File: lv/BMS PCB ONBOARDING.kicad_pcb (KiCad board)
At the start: 4 copper layers, 0 parts

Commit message: UPDATE 6: U1 core placement — VC/CB ladder, balancing staircase, and per-pin rail decoupling
Chip wiring:
- U1 anchored at the centre of the core field, with every bypass cap now
  sitting at the pin it belongs to. LDOIN, NEG5V, AVSS, BAT and CVDD each
  have their cap on the pin, so the loop closes at the pin instead of
  somewhere down a trace.
- The internal-LDO/reference caps (DVDD, TSREF, AVDD, REFHP) came in from
  the far corner of the board toward U1, but they are still not at their
  pins. That is the worst placement problem left on the board.
- Rail rework from UPDATE 5 is now true on the board, checked by net:
    CVDD  = the bulk cap plus the housekeeping pull-ups, the test point
            and the comms connector
    TSREF = the bypass cap and its test point only
- CVDD still has no high-frequency bypass beside its bulk cap, and NFAULT
  still has no pull-up - the test point is the only other pad on that net.

Footprints fixed:
- Nothing to fix: no footprint link on the board changed.
- Carried over from UPDATE 5 and re-verified on the board: the VC/CB sense
  resistor is back on the same hand-solder footprint as the rest of the
  ladder, the common-mode chokes resolve, the Nano-Fit connectors resolve
  to the Nano-Fit footprint, the pre-regulator transistor resolves, and
  every netlist part still resolves.

Blocks on the sheet:
- Whole board re-placed: every footprint moved, none added, none removed,
  netlist unchanged - pure placement, the schematic was not touched.
- Core field around U1 now holds the VC/CB sense resistors, the balancing
  resistors and the ladder caps: the filter and balancing staircase that
  UPDATE 5 could only list as pending.
- Pull-up row consolidated above U1 - the GPIO, ALERT and bus pull-ups
  pulled out of the scatter they were left in, now close to their pins and
  all on CVDD.
- Comms termination left at the connector end, far from U1 - correct, that
  network belongs at the comms conne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
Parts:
- added C1: .47uF, Capacitor_SMD:C_0603_1608Metric, F.Cu at (55.8, 74.8)
- added C10: .47uF, Capacitor_SMD:C_0603_1608Metric, F.Cu at (64.8, 91.2)
- added C11: .47uF, Capacitor_SMD:C_0603_1608Metric, F.Cu at (63.2, 89.5)
- added C12: .47uF, Capacitor_SMD:C_0603_1608Metric, F.Cu at (60.0, 87.5)
- added C19: .47uF, Capacitor_SMD:C_0603_1608Metric, F.Cu at (71.2, 91.2)
- added C2: .47uF, Capacitor_SMD:C_0603_1608Metric, F.Cu at (54.0, 76.3)
- added C20: .47uF, Capacitor_SMD:C_0603_1608Metric, F.Cu at (73.0, 89.5)
- added C201: 10nF, GCM188R72A103KA37J:CAPC1608X90N, F.Cu at (62.3, 70.2)
- added C202: 0.1uF, GCM155R71A104KA55D:CAP_GCM15_1p05X0p55X0p55_MUR-L, F.Cu at (75.2, 76.5)
- added C203: 1uF, C0603C105K8RACAUTO:CAPC18095_95N_KEM-L, F.Cu at (51.9, 57.5)
- added C205: 1uF, C0603C105K8RACAUTO:CAPC18095_95N_KEM-L, F.Cu at (52.9, 59.5)
- added C207: 2.2uF, C0603C105K8RACAUTO:CAPC18095_95N_KEM-L, F.Cu at (51.9, 62.0)
- added C208: 0.1uF, GCM155R71A104KA55D:CAP_GCM15_1p05X0p55X0p55_MUR-L, F.Cu at (74.8, 74.8)
- added C209: 4.7uF, C2012X7R1A475M125AC:CAP_2012_TDK-L, F.Cu at (77.2, 77.1)
- added C21: .47uF, Capacitor_SMD:C_0603_1608Metric, F.Cu at (75.0, 80.0)
- added C210: 1uF, C0603C105K8RACAUTO:CAPC18095_95N_KEM-L, F.Cu at (51.9, 64.2)
- added C22: .47uF, Capacitor_SMD:C_0603_1608Metric, F.Cu at (76.8, 82.5)
- added C23: .47uF, Capacitor_SMD:C_0603_1608Metric, F.Cu at (78.8, 81.0)
- added C24: .47uF, Capacitor_SMD:C_0603_1608Metric, F.Cu at (59.2, 73.5)
- added C25: .47uF, Capacitor_SMD:C_0603_1608Metric, F.Cu at (57.5, 74.9)
- added C26: .47uF, Capacitor_SMD:C_0603_1608Metric, F.Cu at (57.5, 78.2)
- added C27: .47uF, Capacitor_SMD:C_0603_1608Metric, F.Cu at (59.2, 76.8)
- added C28: .47uF, Capacitor_SMD:C_0603_1608Metric, F.Cu at (57.5, 84.7)
- added C29: .47uF, Capacitor_SMD:C_0603_1608Metric, F.Cu at (59.2, 83.3)
- added C3: .47uF, Capacitor_SMD:C_0603_1608Metric, F.Cu at (55.8, 81.2)
- added C30: .47uF, Capacitor_SMD:C_0603_1608Metric, F.Cu at (57.5, 81.5)
- added C31: .47uF, Capacitor_SMD:C_0603_1608Metric, F.Cu at (59.2, 80.0)
- added C32: .47uF, Capacitor_SMD:C_0603_1608Metric, F.Cu at (75.0, 83.5)
- added C33: .47uF, Capacitor_SMD:C_0603_1608Metric, F.Cu at (72.5, 86.0)
- added C34: .47uF, Capacitor_SMD:C_0603_1608Metric, F.Cu at (70.5, 87.8)
- added C35: .47uF, Capacitor_SMD:C_0603_1608Metric, F.Cu at (69.3, 86.0)
- added C36: .47uF, Capacitor_SMD:C_0603_1608Metric, F.Cu at (67.2, 87.8)
- added C37: .47uF, Capacitor_SMD:C_0603_1608Metric, F.Cu at (66.0, 86.0)
- added C38: .47uF, Capacitor_SMD:C_0603_1608Metric, F.Cu at (64.0, 87.8)
- added C39: .47uF, Capacitor_SMD:C_0603_1608Metric, F.Cu at (62.7, 86.0)
- added C4: .47uF, Capacitor_SMD:C_0603_1608Metric, F.Cu at (54.0, 79.5)
- added C40: .47uF, Capacitor_SMD:C_0603_1608Metric, F.Cu at (81.8, 82.8)
- added C41: 470nF, Capacitor_SMD:C_0603_1608Metric, F.Cu at (58.5, 71.0)
- added C5: .47uF, Capacitor_SMD:C_0603_1608Metric, F.Cu at (68.0, 91.2)
- added C6: .47uF, Capacitor_SMD:C_0603_1608Metric, F.Cu at (55.8, 78.0)
- added C602: 0.22uF, GCM31MR72A224KA37L:G-31_MUR-L, F.Cu at (224.3, 70.5)
- added C7: .47uF, Capacitor_SMD:C_0603_1608Metric, F.Cu at (54.0, 82.8)
- added C701: 2200pF, 1206J2K00222KXR:CAPC3216X160N, F.Cu at (229.7, 105.0)
- added C702: 2200pF, 1206J2K00222KXR:CAPC3216X160N, F.Cu at (229.7, 108.4)
- added C703: 220pF, CL10B221JB8NNNC:CAP_CL10_SAM-L, F.Cu at (230.8, 75.0)
- added C704: 220pF, CL10B221JB8NNNC:CAP_CL10_SAM-L, F.Cu at (230.8, 77.2)
- added C705: 220pF, CL10B221JB8NNNC:CAP_CL10_SAM-L, F.Cu at (230.8, 79.4)
- added C706: 220pF, CL10B221JB8NNNC:CAP_CL10_SAM-L, F.Cu at (230.8, 81.6)
- added C707: 2200pF, 1206J2K00222KXR:CAPC3216X160N, F.Cu at (229.7, 111.7)
- added C708: 2200pF, 1206J2K00222KXR:CAPC3216X160N, F.Cu at (229.7, 115.1)
- added C8: .47uF, Capacitor_SMD:C_0603_1608Metric, F.Cu at (69.8, 89.5)
- added C9: .47uF, Capacitor_SMD:C_0603_1608Metric, F.Cu at (66.5, 89.5)
- added D701: 24V, Package_TO_SOT_SMD:SOT-23, F.Cu at (191.9, 107.3)
- added D702: 24V, Package_TO_SOT_SMD:SOT-23, F.Cu at (191.9, 111.7)
- added FL701: 470uH, 744242471:744242471, F.Cu at (226.1, 91.8)
- added FL702: 470uH, 744242471:744242471, F.Cu at (226.1, 98.2)
- added J3: 512810598, FS_4_Global_Footprint_Library:512810598, F.Cu at (224.5, 77.8)
- added J4: 1053131202, FS_4_Global_Footprint_Library:Nanofit-1054301202-1x2SMD90Deg, F.Cu at (203.6, 96.7)
- added J5: 512810598, FS_4_Global_Footprint_Library:512810598, F.Cu at (224.5, 85.1)
- added J6: 1053131202, FS_4_Global_Footprint_Library:Nanofit-1054301202-1x2SMD90Deg, F.Cu at (215.0, 96.7)
- added J701: 430450200, 0430450200:CON_430450200_MOL, F.Cu at (203.8, 63.2)
- added J702: 430450200, 0430450200:CON_430450200_MOL, F.Cu at (215.1, 63.2)
- added Q1: ZXTN25100DGTA, footprintsZXTN25100DGTA:SOT223_DIO, F.Cu at (181.9, 109.8)
- added R1: 10k, Resistor_SMD:R_0805_2012Metric, F.Cu at (72.2, 63.4)
- added R100: 100, Resistor_SMD:R_0805_2012Metric_Pad1.20x1.40mm_HandSolder, F.Cu at (56.2, 97.8)
- added R101: 10, Resistor_SMD:R_2512_6332Metric, F.Cu at (48.5, 90.8)
- added R102: 100, Resistor_SMD:R_0805_2012Metric_Pad1.20x1.40mm_HandSolder, F.Cu at (41.8, 95.0)
- added R103: 100, Resistor_SMD:R_0805_2012Metric_Pad1.20x1.40mm_HandSolder, F.Cu at (41.5, 90.8)
- added R116: 10, Resistor_SMD:R_2512_6332Metric, F.Cu at (73.8, 96.5)
- added R117: 100, Resistor_SMD:R_0805_2012Metric_Pad1.20x1.40mm_HandSolder, F.Cu at (73.8, 103.0)
- added R118: 10, Resistor_SMD:R_2512_6332Metric, F.Cu at (78.0, 96.5)
- added R119: 100, Resistor_SMD:R_0805_2012Metric_Pad1.20x1.40mm_HandSolder, F.Cu at (78.0, 103.0)
- added R12: 5k, Resistor_SMD:R_0805_2012Metric_Pad1.20x1.40mm_HandSolder, F.Cu at (67.8, 63.5)
- added R120: 10, Resistor_SMD:R_2512_6332Metric, F.Cu at (78.8, 87.2)
- added R121: 10, Resistor_SMD:R_2512_6332Metric, F.Cu at (82.2, 96.5)
- added R122: 100, Resistor_SMD:R_0805_2012Metric_Pad1.20x1.40mm_HandSolder, F.Cu at (84.8, 87.2)
- added R123: 100, Resistor_SMD:R_0805_2012Metric_Pad1.20x1.40mm_HandSolder, F.Cu at (82.2, 103.0)
- added R124: 100, Resistor_SMD:R_0805_2012Metric_Pad1.20x1.40mm_HandSolder, F.Cu at (82.2, 77.8)
- added R125: 10, Resistor_SMD:R_2512_6332Metric, F.Cu at (85.5, 79.8)
- added R14: 5k, Resistor_SMD:R_0805_2012Metric_Pad1.20x1.40mm_HandSolder, F.Cu at (63.2, 63.5)
- added R2: 10k, Resistor_SMD:R_0805_2012Metric, F.Cu at (69.6, 58.8)
- added R201: 30, ERJ-3EKF30R0V:RC0603N_PAN-L, F.Cu at (61.5, 72.6)
- added R3: 10k, Resistor_SMD:R_0805_2012Metric, F.Cu at (70.0, 63.5)
- added R4: 10k, Resistor_SMD:R_0805_2012Metric, F.Cu at (63.0, 48.1)
- added R5: 5k, Resistor_SMD:R_0805_2012Metric, F.Cu at (63.0, 51.1)
- added R603: 100, CRCW2010100RFKEF:RES_CRCW_2010-L, F.Cu at (180.1, 116.5)
- added R604: 200, Resistor_SMD:R_2010_5025Metric, F.Cu at (193.2, 116.0)
- added R7: 5k, Resistor_SMD:R_0805_2012Metric, F.Cu at (63.0, 54.0)
- added R701: 0, CRCW08050000Z0EAHP:RES_CRCW_0805_VIS-L, F.Cu at (222.9, 59.4)
- added R702: 0, CRCW08050000Z0EAHP:RES_CRCW_0805_VIS-L, F.Cu at (222.9, 62.1)
- added R703: 0, RC0603JR-070RL:RC0603N_YAG-L, F.Cu at (196.0, 106.1)
- added R704: 0, RC0603JR-070RL:RC0603N_YAG-L, F.Cu at (196.0, 108.2)
- added R705: 0, CRCW08050000Z0EAHP:RES_CRCW_0805_VIS-L, F.Cu at (222.9, 64.9)
- added R706: 0, CRCW08050000Z0EAHP:RES_CRCW_0805_VIS-L, F.Cu at (222.9, 67.6)
- added R707: 51, CRCW060351R0JNEA:RC0603N_VIS-L, F.Cu at (219.0, 77.1)
- added R708: 51, CRCW060351R0JNEA:RC0603N_VIS-L, F.Cu at (219.0, 79.2)
- added R709: 0, CRCW08050000Z0EAHP:RES_CRCW_0805_VIS-L, F.Cu at (226.6, 59.4)
- added R710: 0, CRCW08050000Z0EAHP:RES_CRCW_0805_VIS-L, F.Cu at (226.6, 62.1)
- added R711: 1k, ERJ-3EKF1001V:RC0603N_PAN-L, F.Cu at (219.0, 81.3)
- added R712: 1k, ERJ-3EKF1001V:RC0603N_PAN-L, F.Cu at (219.0, 83.4)
- added R713: 0, CRCW08050000Z0EAHP:RES_CRCW_0805_VIS-L, F.Cu at (226.6, 64.9)
- added R714: 0, CRCW08050000Z0EAHP:RES_CRCW_0805_VIS-L, F.Cu at (226.6, 67.6)
- added R715: 0, CRCW08050000Z0EAHP:RES_CRCW_0805_VIS-L, F.Cu at (230.3, 59.4)
- added R716: 0, CRCW08050000Z0EAHP:RES_CRCW_0805_VIS-L, F.Cu at (230.3, 62.1)
- added R717: 51, CRCW060351R0JNEA:RC0603N_VIS-L, F.Cu at (219.0, 85.5)
- added R718: 51, CRCW060351R0JNEA:RC0603N_VIS-L, F.Cu at (219.0, 87.6)
- added R719: 0, RC0603JR-070RL:RC0603N_YAG-L, F.Cu at (196.0, 110.3)
- added R720: 0, RC0603JR-070RL:RC0603N_YAG-L, F.Cu at (196.0, 112.4)
- added R721: 0, CRCW08050000Z0EAHP:RES_CRCW_0805_VIS-L, F.Cu at (230.3, 64.9)
- added R722: 0, CRCW08050000Z0EAHP:RES_CRCW_0805_VIS-L, F.Cu at (230.3, 67.6)
- added R8: 5k, Resistor_SMD:R_0805_2012Metric, F.Cu at (63.0, 57.0)
- added R80: 100, Resistor_SMD:R_0805_2012Metric_Pad1.20x1.40mm_HandSolder, F.Cu at (53.8, 72.2)
- added R81: 10, Resistor_SMD:R_2512_6332Metric, F.Cu at (59.2, 65.0)
- added R82: 10, Resistor_SMD:R_2512_6332Metric, F.Cu at (48.5, 69.5)
- added R83: 100, Resistor_SMD:R_0805_2012Metric_Pad1.20x1.40mm_HandSolder, F.Cu at (41.5, 69.5)
- added R84: 10, Resistor_SMD:R_2512_6332Metric, F.Cu at (48.5, 82.2)
- added R85: 10, Resistor_SMD:R_2512_6332Metric, F.Cu at (48.5, 78.0)
- added R86: 100, Resistor_SMD:R_0805_2012Metric_Pad1.20x1.40mm_HandSolder, F.Cu at (41.5, 82.2)
- added R87: 100, Resistor_SMD:R_0805_2012Metric_Pad1.20x1.40mm_HandSolder, F.Cu at (41.5, 78.0)
- added R88: 10, Resistor_SMD:R_2512_6332Metric, F.Cu at (65.2, 96.5)
- added R89: 10, Resistor_SMD:R_2512_6332Metric, F.Cu at (48.5, 73.8)
- added R9: 5k, Resistor_SMD:R_0805_2012Metric_Pad1.20x1.40mm_HandSolder, F.Cu at (65.5, 63.5)
- added R90: 10, Resistor_SMD:R_2512_6332Metric, F.Cu at (48.5, 86.5)
- added R91: 100, Resistor_SMD:R_0805_2012Metric_Pad1.20x1.40mm_HandSolder, F.Cu at (41.5, 73.7)
- added R92: 100, Resistor_SMD:R_0805_2012Metric_Pad1.20x1.40mm_HandSolder, F.Cu at (41.5, 86.5)
- added R93: 10, Resistor_SMD:R_2512_6332Metric, F.Cu at (69.5, 96.5)
- added R94: 100, Resistor_SMD:R_0805_2012Metric_Pad1.20x1.40mm_HandSolder, F.Cu at (69.5, 103.0)
- added R95: 10, Resistor_SMD:R_2512_6332Metric, F.Cu at (61.0, 96.5)
- added R96: 100, Resistor_SMD:R_0805_2012Metric_Pad1.20x1.40mm_HandSolder, F.Cu at (65.2, 103.0)
- added R97: 10, Resistor_SMD:R_2512_6332Metric, F.Cu at (56.2, 91.5)
- added R98: 100, Resistor_SMD:R_0805_2012Metric_Pad1.20x1.40mm_HandSolder, F.Cu at (61.0, 103.0)
- added R99: 10, Resistor_SMD:R_2512_6332Metric, F.Cu at (48.5, 95.0)
- added TP501: 5012, 5012:TP_5012, F.Cu at (215.0, 105.7)
- added TP502: 5012, 5012:TP_5012, F.Cu at (215.0, 110.4)
- added TP503: 5012, 5012:TP_5012, F.Cu at (215.0, 115.1)
- added TP504: 5012, 5012:TP_5012, F.Cu at (219.8, 105.7)
- added TP505: 5012, 5012:TP_5012, F.Cu at (219.8, 110.4)
- added TP506: 5012, 5012:TP_5012, F.Cu at (219.8, 115.1)
- added TP507: 5012, 5012:TP_5012, F.Cu at (224.5, 105.7)
- added TP508: 5012, 5012:TP_5012, F.Cu at (224.5, 110.4)
- added TP509: 5012, 5012:TP_5012, F.Cu at (224.5, 115.1)
- added U1: BQ79616PAPRQ1, footprintsBQ79616PAPRQ1:PAP0064F-IPC_A, F.Cu at (67.3, 78.0)

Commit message: UPDATE 7: board edge and mounting holes — connector half brought in as blocks
Board edge:
- The outline is on the board now, drawn as straight runs and rounded corners.
  Before this the file had no Edge.Cuts geometry at all, which is why DRC could
  not start and nothing could be plotted.
- The top-right corner is cut away: the area beyond the notch line is off the
  board, so the outline is not a plain rectangle.
- Every corner is an arc, and each mounting hole sits at the centre of one, so
  the corner relief is concentric with the fastener rather than cut beside it.
- Not closed yet: the right edge stops just short of where the next run picks
  it up, and a short segment lies on the left edge duplicating that part of it.
  Both leave free endpoints, which is what the outline check and every plot key
  off. The break is closed in the newer autosave; the duplicated segment is in
  all of them.

Mounting:
- The mounting holes are non-plated: a bare drill with no annular ring, and
  excluded from the BOM. At the tightest corners the ligament to the edge is
  thin but real; a washer up to the size the corner relief allows sits inside
  the arc, and anything wider overhangs it.
- Added on the sheet as well as the board - mounting-hole symbols with their
  own references - so schematic and board still agree after the board gained
  its footprints, and the used-designator list picked them up.

Blocks on the sheet:
- The connector / daisy-chain half came in from the far side of the sheet:
  a large share of the board moved and many parts also rotated between the
  first snapshot of the evening and the later save, most of them from
  beyond the right-hand end of the drawing area.
- The isolated block then moved as one piece: its parts - both daisy-chain
  connectors, the ladder resistors, the filter caps, the TVS pair and the
  chokes - shifted by a single rigid offset, with nothing inside the block
  changing relative to anything else in it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
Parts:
- added H1: MountingHole, MountingHole:MountingHole_2.5mm, F.Cu at (20.8, 30.2)
- added H2: MountingHole, MountingHole:MountingHole_2.5mm, F.Cu at (21.0, 107.5)
- added H3: MountingHole, MountingHole:MountingHole_2.5mm, F.Cu at (107.5, 52.0)
- added H4: MountingHole, MountingHole:MountingHole_2.5mm, F.Cu at (130.8, 107.5)
- moved R721 194.5 mm to (38.0, 36.2)
- moved R722 194.5 mm to (38.0, 39.0)
- moved C707 193.4 mm to (52.0, 35.6)
- moved C708 193.4 mm to (52.0, 39.0)
- moved FL702 191.5 mm to (44.5, 37.4)
- moved R715 187.7 mm to (44.5, 33.2), turned to 180 degrees
- moved R716 187.0 mm to (44.4, 41.5), turned to 180 degrees
- moved J702 186.1 mm to (30.5, 39.9)
- moved R701 185.1 mm to (37.8, 54.5), turned to 180 degrees
- moved R702 185.1 mm to (37.9, 57.2), turned to 180 degrees
- moved FL701 184.9 mm to (44.7, 55.9)
- moved C701 184.8 mm to (52.0, 54.4)
- moved C702 184.8 mm to (52.0, 57.8)
- moved R705 178.7 mm to (44.7, 52.0), turned to 180 degrees
- moved R706 178.1 mm to (44.9, 60.0), turned to 180 degrees
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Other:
- board outline added: 117.8 x 85.2 mm

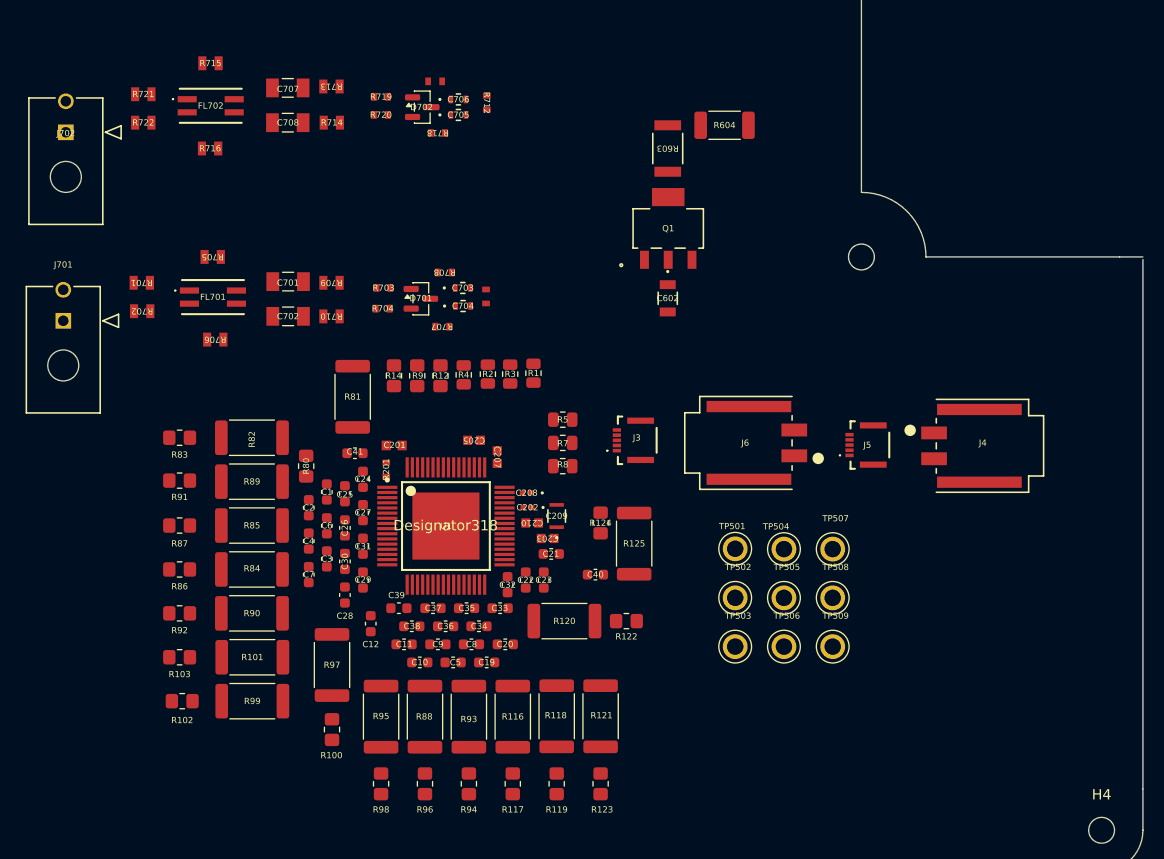
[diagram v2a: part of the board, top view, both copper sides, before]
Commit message: UPDATE 8: Finished routing and placement
Routing:
- Everything the outline was waiting for arrived: the ladder, the sense and tap
  junctions, the cell-tab chain, the ground escapes, the pack top, the
  pre-regulator pass path, the balance feedback, the host bus and status lines,
  the GPIO terminations, and the isolated half from the transceiver pins
  through the option links, isolation capacitors, chokes and TVS pair out to
  the daisy-chain connectors. The saved board is routed apart from two nets.
- Only three widths exist on the whole board and no others: the thin sense
  width on the cell sense and tab junctions, the default width on the balance
  runs, the bus, the reference rails, the GPIO terminations and the whole
  comms channel, and the wide power width on the pre-regulator, the pack top
  and the ground escapes.
- Every one of those was picked by hand. The net classes are still unassigned,
  so nothing enforces any of it, and the custom rules file was emptied during
  the session as well - there is no rule check behind any width on this board.
- The pre-regulator carries its pass device and a guard around it on the wide
  width, so the one high-current path got the one width that matters.

Planes and layers:
- The pours went through three states: a first set of ground patches was
  poured, deleted, and replaced by a single ground pour on the reserved plane
  layer.
- In every version, including the save, the pour does not cover the monitor
  IC's exposed pad. The device reaches ground only through its own traces and a
  handful of vias rather than flooding into the plane.
- The other plane layer has never carried copper - checked across the whole of
  local history, it is empty in all of it. So the longest sense runs and the
  entire comms channel sit on the back layer with no reference under them: the
  only plane in the board is above them with the empty layer in between.

Rule areas are not pours:
- The green hatched a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
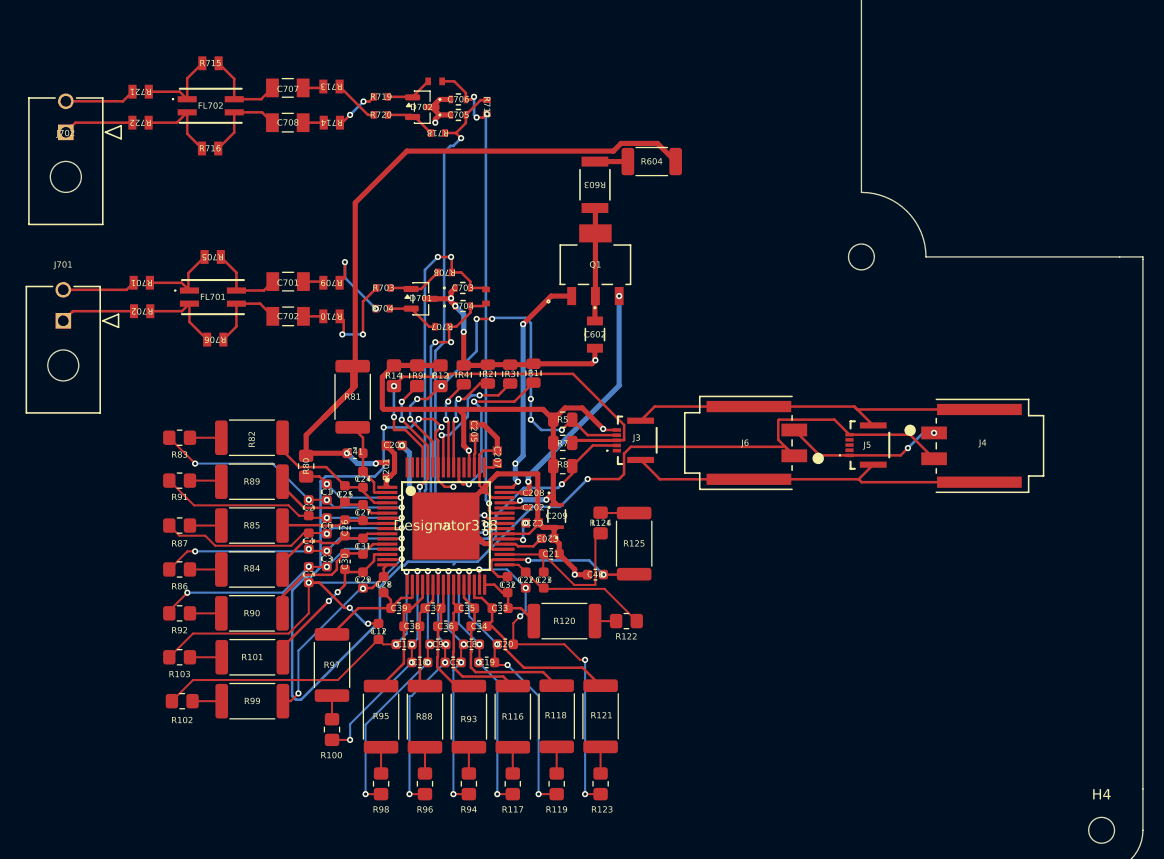
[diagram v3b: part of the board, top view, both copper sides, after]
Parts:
- removed TP501, TP502, TP503, TP504, TP505, TP506, TP507, TP508, TP509: 5012, 5012:TP_5012
- moved C602 7.87 mm to (81.7, 59.5)
- moved Q1 7.87 mm to (81.8, 52.8)
- moved R603 7.87 mm to (81.7, 45.0)
- moved R604 7.87 mm to (87.2, 42.8)
- moved C28 3.88 mm to (61.2, 83.7)
- moved C12 1.06 mm to (60.8, 88.2)
- moved C205 0.87 mm to (70.0, 68.9), turned to -90 degrees
- moved C208 0.66 mm to (75.8, 74.8)
- moved C202 0.58 mm to (75.8, 76.2)
- moved R712 0.43 mm to (71.2, 37.5)
- moved R721 0.36 mm to (37.7, 36.0), turned to 180 degrees
- moved R722 0.27 mm to (37.7, 39.0), turned to 180 degrees
- turned R714 to 180 degrees
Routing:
- net DQ: track 0.00 -> 129.6 mm, vias 0 -> 5
- net AVSS: track 0.00 -> 88.2 mm, vias 0 -> 8
- net BAT: track 0.00 -> 75.0 mm, vias 0 -> 2
- net (no net): track 0.00 -> 71.8 mm
- net CVDD: track 0.00 -> 53.0 mm, vias 0 -> 4
- net COMHN: track 0.00 -> 51.1 mm, vias 0 -> 2
- net COMHP: track 0.00 -> 47.7 mm, vias 0 -> 4
- net I2C_SDA: track 0.00 -> 45.5 mm, vias 0 -> 2
- net COMLN: track 0.00 -> 44.0 mm, vias 0 -> 3
- net ALERT: track 0.00 -> 43.1 mm, vias 0 -> 8
- net I2C_SCL: track 0.00 -> 41.1 mm, vias 0 -> 4
- net Net-(U1-VC10): track 0.00 -> 38.0 mm, vias 0 -> 4
- net Net-(U1-VC2): track 0.00 -> 34.7 mm, vias 0 -> 5
- net COMLP: track 0.00 -> 33.3 mm, vias 0 -> 3
- net Net-(U1-VC9): track 0.00 -> 33.1 mm, vias 0 -> 2
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- added copper zone on In1.Cu, net AVSS

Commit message: FINAL UPDATE: NO DRC OR ERC ERRORS REMAINING
Routing:
- The inner-layer AVSS zone was pinched across one horizontal line by the clearance holes of nearby CVDD, LDOIN and AVDD vias.
- That cut the zone into two islands, so the upper AVSS network had no link into the main plane.
- KiCad reported this as the single unconnected item on the board.
- Added one AVSS stitching via on the existing front-layer AVSS trace, where it drops into the main zone.
- Refilled the zone so the via bridges the two islands.
- Result: the unconnected item is gone.

Solder mask bridges (ten errors)
- Twelve front-layer track segments had no net.
- They ran between the unassigned mechanical mounting pads of J3, J4, J5 and J6.
- Each pad-to-track junction raised a solder mask bridge error.
- The segments carried no electrical function.
- Removed all twelve; the mounting pads themselves were not changed.
- Result: the ten solder mask bridge errors are gone.

Connector pad clearance (eight errors)
- J3 and J5 are 0.5 mm pitch connectors with 0.35 mm pads, leaving a 0.15 mm gap.
- The board's default clearance is 0.18 mm, so pins 1 to 5 on both failed.
- Set a 0.15 mm pad clearance override on those pins.
- Applied it in the board and in the connector's library footprint, so a footprint refresh keeps it.
- Result: the eight clearance errors are gone.

Resistor courtyards (96 errors)
- Twelve 0805 resistors each had twelve courtyard lines instead of four.
- Some lines were zero-length; others overlapped as collinear stubs, so no closed outline formed.
- Replaced each set with one closed rectangle.
- Applied it in the board and in the library footprint.
- Result: the 96 malformed courtyard errors are gone.

DRC verification
- The error-level DRC run on the saved board reports zero errors and zero unconnected items, exit code 0.
- The changes are in commit 70d4d6f on main.
- The board is still open in KiCad with its editor lock; reload it from disk before saving.
-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
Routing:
- net (no net): track 71.8 -> 0.00 mm
- net AVSS: vias 8 -> 9
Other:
- outline, holes or cut-outs redrawn
